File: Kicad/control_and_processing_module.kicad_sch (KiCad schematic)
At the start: 42 parts, among them J1 Micro_SD_Card, J2 Conn_Coaxial, J3 Conn_01x06, J4 USB_C_Receptacle_USB2.0_16P, SW1 SW_Push, SW2 SW_Push, U1 STM32WB55RGVx, U2 USBLC6-2SC6, U6 LM1117DT-3.3, X1 32.768kHz, X2 32MHz

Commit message: Más avances en el esquemático en Kicad.
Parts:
- removed C1, C10, C15, C16, C2, C3, C4, C5, C6, C9: 100n, symbol Device:C
- removed C11, C12: C, symbol Device:C
- removed C13: 0p8, symbol Device:C
- removed C14: 0p3, symbol Device:C
- removed C36, C37: 10u, symbol Device:C
- removed C7, C8: 4u7, symbol Device:C
- removed D1: LED, symbol Device:LED
- removed D4, D5: B560C, symbol Device:D_Schottky
- removed FLT1: DLF162500LT-5028A1, equipo_medicion_ensayo_celdas_footprints:DLF162500LT-5028A1, symbol equipo_medicion_ensayo_celdas_sch_symbols:DLF162500LT-5028A1
- removed J1: Micro_SD_Card, symbol Connector:Micro_SD_Card
- removed J2: Conn_Coaxial, symbol Connector:Conn_Coaxial
- removed J3: Conn_01x06, Connector_PinHeader_2.54mm:PinHeader_1x06_P2.54mm_Vertical, symbol Connector_Generic:Conn_01x06
- removed J4: USB_C_Receptacle_USB2.0_16P, symbol Connector:USB_C_Receptacle_USB2.0_16P
- removed L1: 2n7, symbol Device:L
- removed R1, R3, R4: 5K1, symbol Device:R
- removed R18, R19, R20: 10k, symbol Device:R
- removed R2, R6: 220, symbol Device:R
- removed SW1, SW2: SW_Push, symbol Switch:SW_Push
- removed U1: STM32WB55RGVx, Package_DFN_QFN:QFN-68-1EP_8x8mm_P0.4mm_EP6.4x6.4mm, symbol MCU_ST_STM32WB:STM32WB55RGVx
- removed U2: USBLC6-2SC6, Package_TO_SOT_SMD:SOT-23-6, symbol Power_Protection:USBLC6-2SC6
- removed U6: LM1117DT-3.3, Package_TO_SOT_SMD:TO-252-3_TabPin2, symbol Regulator_Linear:LM1117DT-3.3
- removed X1: 32.768kHz, symbol Device:Crystal
- removed X2: 32MHz, symbol Device:Crystal_GND24_Small
- added C34, C43: 4u7, symbol Device:C
- added C35, C40, C41, C42, C44, C45, C46, C47, C49, C51: 100n, symbol Device:C
- added C38, C39: 10u, symbol Device:C
- added C48, C50: C, symbol Device:C
- added C52: 0p8, symbol Device:C
- added C53: 0p3, symbol Device:C
- added D6, D7: B560C, symbol Device:D_Schottky
- added D8: LED, symbol Device:LED
- added FLT2: DLF162500LT-5028A1, equipo_medicion_ensayo_celdas_footprints:DLF162500LT-5028A1, symbol equipo_medicion_ensayo_celdas_sch_symbols:DLF162500LT-5028A1
- added J5: USB_C_Receptacle_USB2.0_16P, symbol Connector:USB_C_Receptacle_USB2.0_16P
- added J6: Conn_01x06, Connector_PinHeader_2.54mm:PinHeader_1x06_P2.54mm_Vertical, symbol Connector_Generic:Conn_01x06
- added J7: Conn_Coaxial, symbol Connector:Conn_Coaxial
- added J8: Micro_SD_Card, symbol Connector:Micro_SD_Card
- added L4: 2n7, symbol Device:L
- added R21, R22, R24: 5K1, symbol Device:R
- added R23, R25: 220, symbol Device:R
- added R26, R27, R28: 10k, symbol Device:R
- added SW3, SW4: SW_Push, symbol Switch:SW_Push
- added U5: USBLC6-2SC6, Package_TO_SOT_SMD:SOT-23-6, symbol Power_Protection:USBLC6-2SC6
- added U7: LM1117DT-3.3, Package_TO_SOT_SMD:TO-252-3_TabPin2, symbol Regulator_Linear:LM1117DT-3.3
- added U8: STM32WB55RGVx, Package_DFN_QFN:QFN-68-1EP_8x8mm_P0.4mm_EP6.4x6.4mm, symbol MCU_ST_STM32WB:STM32WB55RGVx
- added X3: 32.768kHz, symbol Device:Crystal
- added X4: 32MHz, symbol Device:Crystal_GND24_Small
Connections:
- net +3V3: now also C34.1, C35.1, C39.1, C40.1, C41.1, C42.1, C43.1, C44.1, C45.1, C46.1, C47.1, J6.1 (Pin_1), J8.4 (VDD), R26.1, R27.1, R28.1, SW3.2, U7.2 (VO), U8.1 (VBAT), U8.14 (VDDA), U8.30 (VDD), U8.33 (VDDRF), U8.41 (VFBSMPS), U8.43 (VLXSMPS), U8.44 (VDDSMPS), U8.45 (VDD), U8.55 (VDDUSB), U8.68 (VDD)
- net BOOT0: now also C49.1, R24.1, R25.1, U8.5 (PH3)
- net GND: now also C34.2, C35.2, C38.2, C39.2, C40.2, C41.2, C42.2, C43.2, C44.2, C45.2, C46.2, C47.2, C48.2, C49.2, C50.2, C51.2, C52.2, C53.2, FLT2.2 (GND), FLT2.4 (GND), J5.A1 (GND), J5.A12 (GND), J5.B1 (GND), J5.B12 (GND), J5.S1 (SHIELD), J6.6 (Pin_6), J7.2 (Ext), J8.6 (VSS), R21.2, R22.2, R23.1, R24.2, U5.2 (GND), U7.1 (GND), U8.32 (VSSRF), U8.42 (VSSSMPS), U8.69 (VSS), X4.2, X4.4
- net HSE_IN: now also U8.35 (OSC_IN), X4.1
- net HSE_OUT: now also U8.34 (OSC_OUT), X4.3
- net LED_K: now also D8.1 (K), R23.2
- net LSE_IN: now also C50.1, U8.3 (PC14), X3.2
- net LSE_OUT: now also C48.1, U8.4 (PC15), X3.1
- net MISO: now also J8.3 (CMD), J8.7 (DAT0), R27.2, R28.2, U8.48 (PB14), U8.49 (PB15)
- net RF: now also C52.1, L4.1, U8.31 (RF1)
- net RF_ANT: now also FLT2.3 (OUT), J7.1 (In)
- net RF_MATCH: now also C53.1, FLT2.1 (IN), L4.2
- net SD_CS: now also J8.2 (DAT3/CD), R26.2, U8.7 (PB9)
- net SD_SCK: now also J8.5 (CLK), U8.47 (PB13)
- net SWCLK: now also J6.3 (Pin_3), U8.56 (PA14)
- net SWDIO: now also J6.4 (Pin_4), U8.54 (PA13)
- net SWD_NRST: now also C51.1, J6.2 (Pin_2), SW4.1, U8.8 (NRST)
- net SWO: now also J6.5 (Pin_5), U8.63 (PB3)
- net USB_D+: now also U5.4 (I/O2), U8.53 (PA12)
- net USB_D-: now also U5.6 (I/O1), U8.52 (PA11)
- net VBUS: now also D6.2 (A), J5.A4 (VBUS), J5.A9 (VBUS), J5.B4 (VBUS), J5.B9 (VBUS), U5.5 (VBUS)
- new net: J5.A7 (D-), J5.B7 (D-), U5.1 (I/O1)
- new net: J5.A6 (D+), J5.B6 (D+), U5.3 (I/O2)
- new net: R25.2, SW3.1
- new net: J5.B5 (CC2), R21.1
- new net: C38.1, D6.1 (K), D7.1 (K), U7.3 (VI)
- new net: J5.A5 (CC1), R22.1
- new net: D8.2 (A), U8.22 (PA7)
- new net +5V_IN: D7.2 (A)
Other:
- removed sheet CONTROL_AND_PROCESSING
- removed sheet POWER_IN
- title: Placa prueba BQ24780s -> (none)

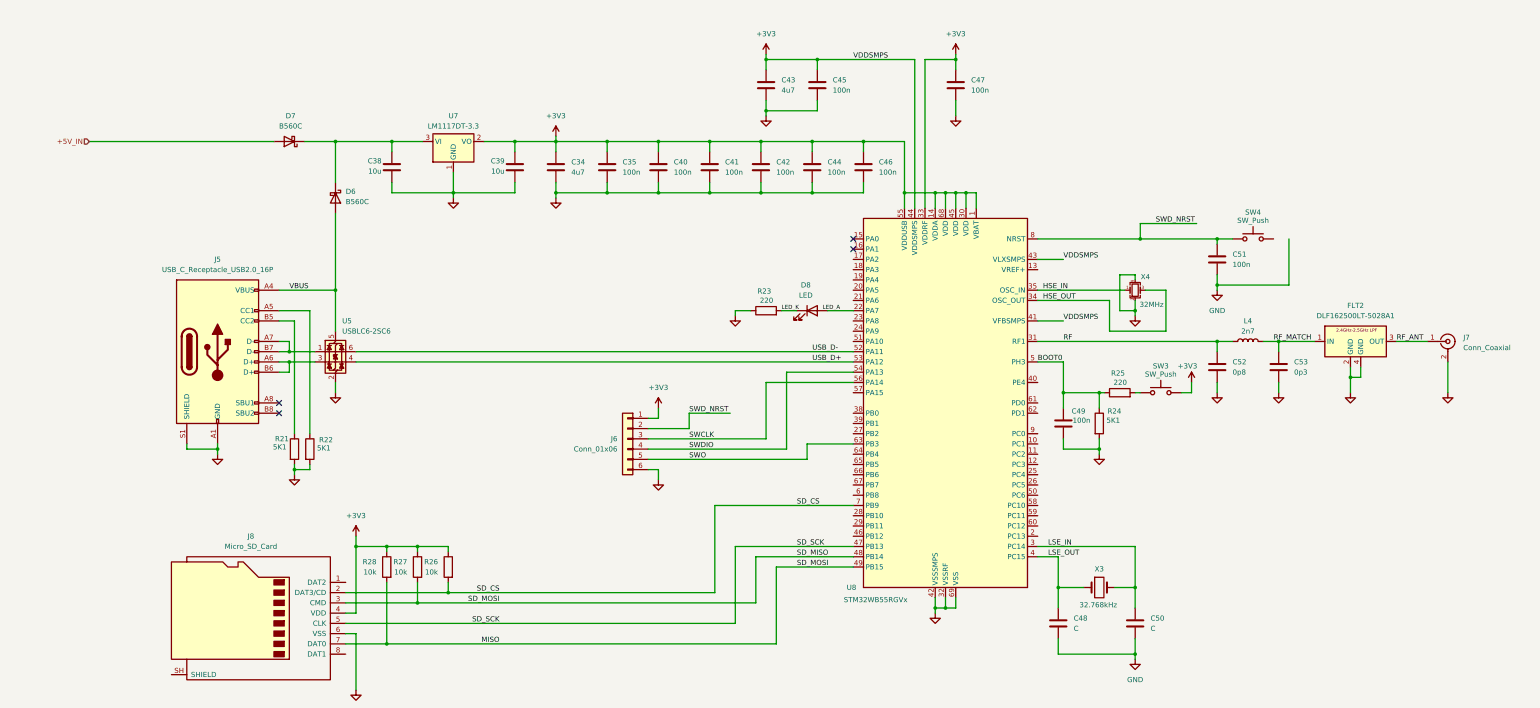
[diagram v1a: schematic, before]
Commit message: Avances en fuente partida del esquemático Kicad.
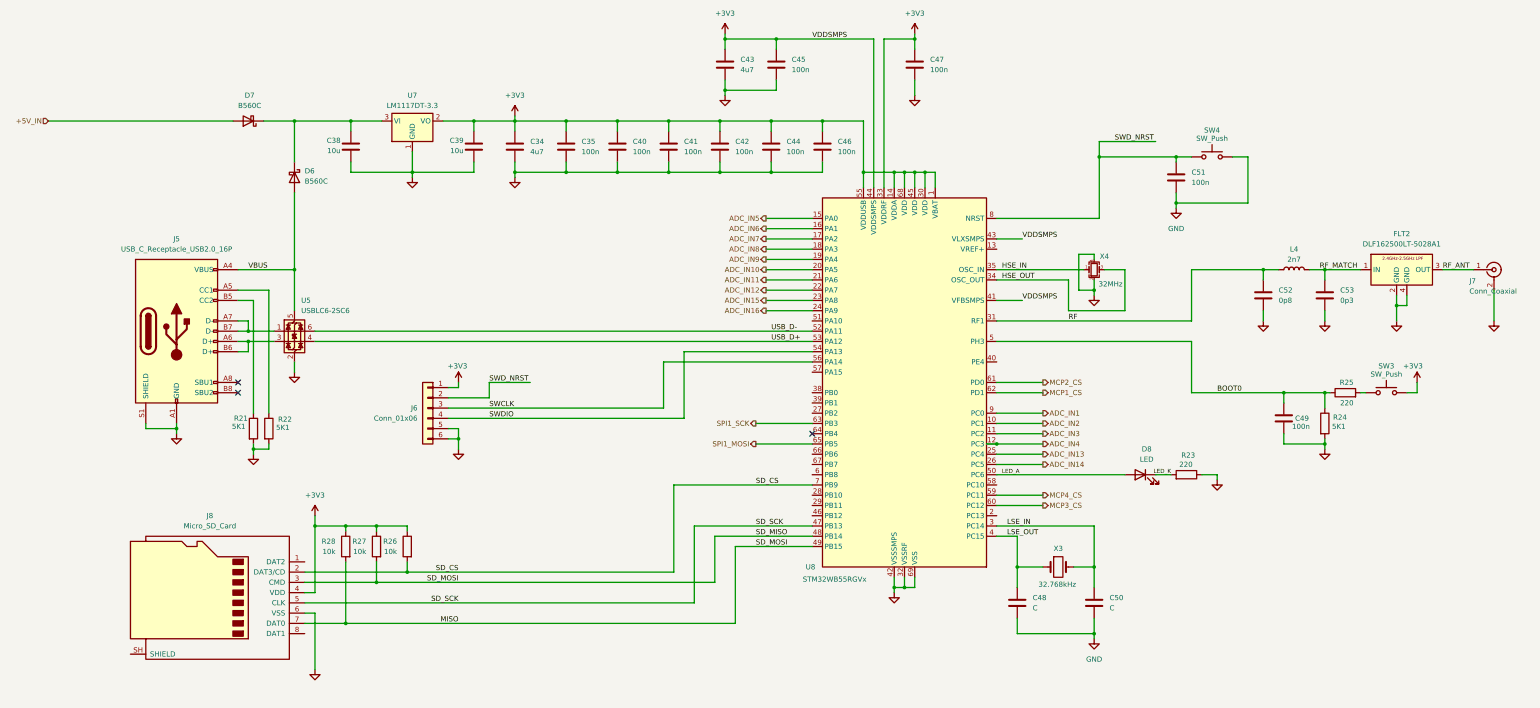
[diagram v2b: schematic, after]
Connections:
- net GND: now also J6.5 (Pin_5), SW4.2
- net LED_A: now also D8.2 (A), U8.50 (PC6)
- net ADC_IN2: now reaches U8.10 (PC1)
- net ADC_IN3: now reaches U8.11 (PC2)
- net ADC_IN4: now reaches U8.12 (PC3)
- net ADC_IN5: now reaches U8.15 (PA0)
- net ADC_IN6: now reaches U8.16 (PA1)
- net ADC_IN7: now reaches U8.17 (PA2)
- net ADC_IN8: now reaches U8.18 (PA3)
- net ADC_IN9: now reaches U8.19 (PA4)
- net ADC_IN10: now reaches U8.20 (PA5)
- net ADC_IN11: now reaches U8.21 (PA6)
- net ADC_IN12: now reaches U8.22 (PA7)
- net ADC_IN12: no longer D8.2 (A)
- net ADC_IN15: now reaches U8.23 (PA8)
- net ADC_IN16: now reaches U8.24 (PA9)
- net ADC_IN13: now reaches U8.25 (PC4)
- net ADC_IN14: now reaches U8.26 (PC5)
- net MCP4_CS: now reaches U8.59 (PC11)
- net MCP3_CS: now reaches U8.60 (PC12)
- net MCP2_CS: now reaches U8.61 (PD0)
- net MCP1_CS: now reaches U8.62 (PD1)
- net SPI1_MOSI: now reaches U8.65 (PB5)
- net ADC_IN1: now reaches U8.9 (PC0)
- net SWO renamed SPI1_SCK
- net SPI1_SCK: no longer J6.5 (Pin_5)
- no-connect marks 4 -> 3
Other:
- moved on the sheet: C34, C35, C38, C39, C40, C41, C42, C43, C44, C45, C46, C47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

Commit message: Pruebas y avances en FW principal y relacionadas a lecturas de ADCs.
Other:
- note added: "Conectar a REF3333"
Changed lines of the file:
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@@
 	(generator_version "10.0")
 	(paper "A3")
+	(text "Conectar a REF3333"
+		(exclude_from_sim no)
+		(at 278.13 115.824 0)
+		(effects
+			(font
+				(size 1.27 1.27)
+			)
+		)
+	)
 	(junction
 		(at 247.65 96.52)
